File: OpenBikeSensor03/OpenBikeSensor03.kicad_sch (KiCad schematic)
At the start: 24 parts, among them J1 Battery, J2 GPS, J3 Sensor 1, J4 Sensor 2, J5 Display Cable, J6 Ein/Aus-Schalter, J7 SD_Card, J8 Addons, M1 LIPoChargerwithProtection, U1 ESP32 WROOM 30-Pin, U4 DCDC_fix

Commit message: More simplification
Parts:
- C2, C3: footprint Capacitors_THT:CP_Radial_D4.0mm_P1.50mm -> Custom_Modules:CP_Radial_D4.0mm_P1.50mm
- F1: footprint Fuse_Holders_and_Fuses:Fuse_TE5_Littlefuse-395Series -> Custom_Modules:Fuse
- J1: footprint Connector_PinHeader_2.54mm:PinHeader_1x02_P2.54mm_Vertical -> Custom_Modules:Connector_1x02
- J2: renamed from J6; footprint Connector_PinHeader_2.54mm:PinHeader_1x02_P2.54mm_Vertical -> Custom_Modules:Connector_1x02
- U1: footprint ESP32-DEVKITC-32D:MODULE_ESP32-DEVKITC-32C_SMDBACKUP -> ESP32-DEVKITC-32D:MODULE_ESP32-DEVKITC-32C_SMD_BOTH
- U2: renamed from U4; footprint Custom_Modules:MT3608_SEPIC_DCDC -> Custom_Modules:MT3608_SEPIC_DCDC_SMD
- renumbered D2 to D1, H3 to H1, H1 to H3, J7 to J5, J2 to J6, J5 to J7, R2 to R1, R3 to R2, R1 to R3, R6 to R4, R7 to R5
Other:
- note added: "Add-ons"
- note added: "Befestigungslöcher"
- note added: "Spannungsteiler zur Messung der Batteriespannung"
- note removed: "Addons"
- moved on the sheet: H1, H3, J1, J2

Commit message: clean up libraries
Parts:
- J2: value Ein/Aus-Schalter -> On/Off
- J3, J4: footprint Connector_PinHeader_2.54mm:PinHeader_1x04_P2.54mm_Vertical -> Custom_Modules:Connector_1x04
- J5: renamed from J7; footprint Connector_JST:JST_XH_B5B-XH-AM_1x05_P2.50mm_Vertical -> Custom_Modules:Connector_1x05_Display
- J6: renamed from J8; value Addons -> Add-ons; footprint Connector_PinHeader_2.54mm:PinHeader_1x06_P2.54mm_Vertical -> Custom_Modules:Connector_1x06
- M1: renamed from U1; footprint ESP32-DEVKITC-32D:MODULE_ESP32-DEVKITC-32C_SMD_BOTH -> Custom_Modules:ESP32_WROOM_30_SMD; symbol ESP32-DEVKITC-32D:ESP32-DEVKIT-32C -> Custom_Module:ESP32-WROOM-30
- M2: renamed from M1; symbol Custom_Module:LIPoChargerwithProtection -> Custom_Module:LIPoChargerWithProtection
- M3: renamed from U2; symbol DCDC_Converter:DCDC_fix -> Custom_Module:VoltageRegulator
- M4: renamed from J5; value SD_Card -> SD; footprint Connector_PinHeader_2.54mm:PinHeader_1x06_P2.54mm_Vertical -> Custom_Modules:Connector_1x06
- M5: renamed from J6; footprint Connector_PinHeader_2.54mm:PinHeader_1x04_P2.54mm_Vertical -> Custom_Modules:Connector_1x04
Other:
- note added: "Bulk decoupling, place near ESP32 and display cable connector"
- note added: "DC/DC voltage regulator (red module)"
- note added: "Distance Sensors"
- note added: "GPS Module"
- note added: "I2C pull up resistors"
- note added: "IN=USB Voltage, not used"
- note added: "LiPo Charger and Protection (blue module)"
- note added: "Mounting"
- note added: "Mounting holes"
- note added: "Passives"
- note added: "Power"
- note added: "SD Card Module"
- note added: "The addon port can be used for hacking the device and adding custom extensions, or while debugging. It exposes 3.3V power, the I2C bus and the RX/TX lines for serial output and communications."
- note added: "Voltage divider for measuring battery voltage via ADC pin"
- note added: "pull down resistor for button"
- note removed: "Befestigung"
- note removed: "Befestigungslöcher"
- note removed: "Entkopplung, platzieren in Nähe von ESP32 und Displaystecker"
- note removed: "GPS-Modul"
- note removed: "I2C Pull-Ups"
- note removed: "IN+/IN- ist die USB Bus-Spannung und wird nicht verwendet"
- note removed: "Laderegler & Batterieschutz (blaues Modul)"
- note removed: "Passive Bauteile"
- note removed: "Pull-Down Button"
- note removed: "SD-Karte"
- note removed: "Sensoren"
- note removed: "Spannungsregler (rotes Modul)"
- note removed: "Spannungsteiler zur Messung der Batteriespannung"
- note removed: "Stromversorgung"
- moved on the sheet: C1, C2, C3, D1, F1, H1, H2, H3, J1, J2, J3, J4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

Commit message: rename custom libraries to "OpenBikeSensor"
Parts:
- C2, C3: footprint Custom_Modules:CP_Radial_D4.0mm_P1.50mm -> OpenBikeSensor:CP_Radial_D4.0mm_P1.50mm
- F1: footprint Custom_Modules:Fuse -> OpenBikeSensor:Fuse
- J1, J2: footprint Custom_Modules:Connector_1x02 -> OpenBikeSensor:Connector_1x02
- J3, J4, M5: footprint Custom_Modules:Connector_1x04 -> OpenBikeSensor:Connector_1x04
- J5: footprint Custom_Modules:Connector_1x05_Display -> OpenBikeSensor:Connector_1x05_Display
- J6, M4: footprint Custom_Modules:Connector_1x06 -> OpenBikeSensor:Connector_1x06
- M1: footprint Custom_Modules:ESP32_WROOM_30_SMD -> OpenBikeSensor:ESP32_WROOM_30_SMD; symbol Custom_Module:ESP32-WROOM-30 -> OpenBikeSensor:ESP32-WROOM-30
- M2: footprint Custom_Modules:BATTERY-CHARGER-LI-PROT -> OpenBikeSensor:BATTERY-CHARGER-LI-PROT; symbol Custom_Module:LIPoChargerWithProtection -> OpenBikeSensor:LIPoChargerWithProtection
- M3: footprint Custom_Modules:MT3608_SEPIC_DCDC_SMD -> OpenBikeSensor:MT3608_SEPIC_DCDC_SMD; symbol Custom_Module:VoltageRegulator -> OpenBikeSensor:VoltageRegulator
- R1, R2, R3, R4, R5: footprint Custom_Modules:Resistor_Combined_THT3_SMD0805 -> OpenBikeSensor:Resistor_Combined_THT3_SMD0805

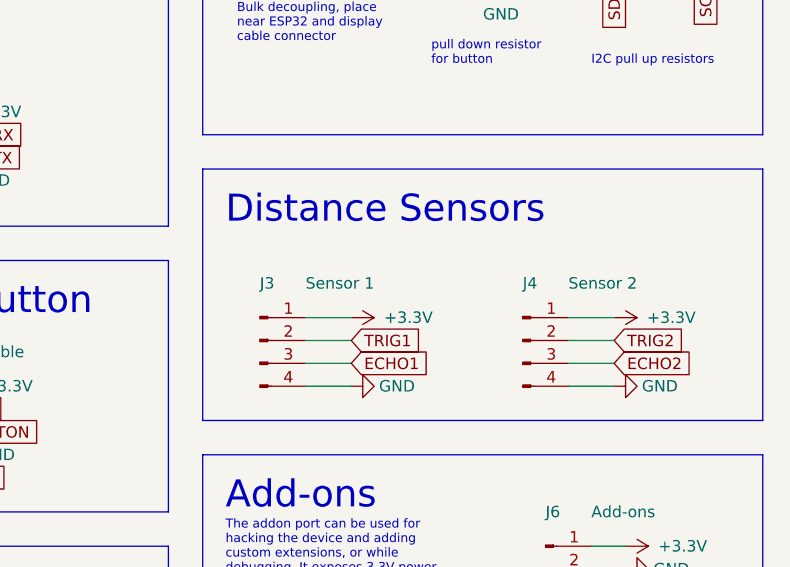
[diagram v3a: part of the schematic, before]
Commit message: Rename sensor module connectors to S1/S2
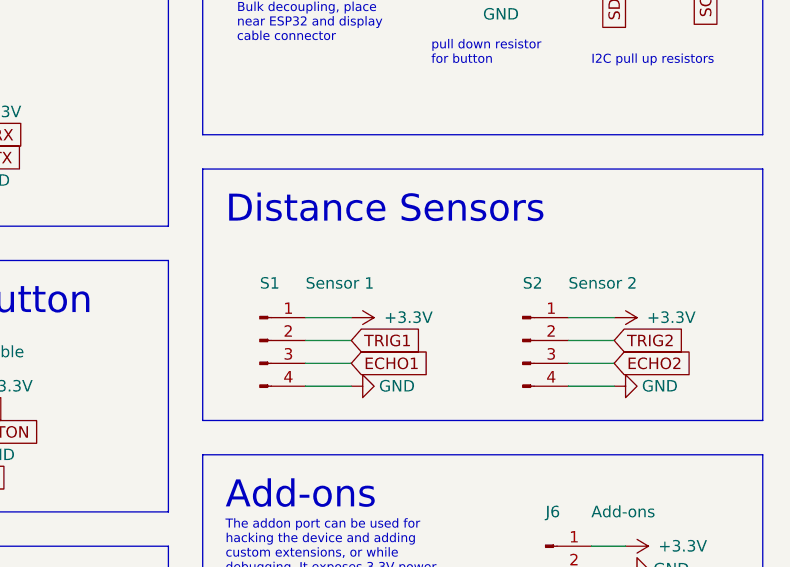
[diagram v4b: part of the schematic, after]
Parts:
- renumbered J3 to S1, J4 to S2
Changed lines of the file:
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@@
   (symbol (lib_id "Connector:Conn_01x04_Male") (at 212.09 101.6 0) (unit 1)
     (in_bom yes) (on_board yes)
-    (property "Reference" "J3" (id 0) (at 212.09 95.25 0)
+    (property "Reference" "S1" (id 0) (at 212.09 95.25 0)
       (effects (font (size 1.27 1.27)) (justify left))
     )
@@
   (symbol (lib_id "Connector:Conn_01x04_Male") (at 241.3 101.6 0) (unit 1)
     (in_bom yes) (on_board yes)
-    (property "Reference" "J4" (id 0) (at 241.3 95.25 0)
+    (property "Reference" "S2" (id 0) (at 241.3 95.25 0)
       (effects (font (size 1.27 1.27)) (justify left))
     )
@@
       (reference "J2") (unit 1) (value "On/Off") (footprint "OpenBikeSensor:Connector_1x02")
     )
-    (path "/00000000-0000-0000-0000-00005ed6a6b4"
-      (reference "J3") (unit 1) (value "Sensor 1") (footprint "OpenBikeSensor:Connector_1x04")
-    )
-    (path "/00000000-0000-0000-0000-00005ed6b21f"
-      (reference "J4") (unit 1) (value "Sensor 2") (footprint "OpenBikeSensor:Connector_1x04")
-    )
     (path "/00000000-0000-0000-0000-00005ed82c02"
       (reference "J5") (unit 1) (value "Display Cable") (footprint "OpenBikeSensor:Connector_1x05_Display")
@@
       (reference "R5") (unit 1) (value "1k2") (footprint "OpenBikeSensor:Resistor_Combined_THT3_SMD0805")
     )
-  )
+    (path "/00000000-0000-0000-0000-00005ed6a6b4"
+      (reference "S1") (unit 1) (value "Sensor 1") (footprint "OpenBikeSensor:Connector_1x04")
+    )
+    (path "/00000000-0000-0000-0000-00005ed6b21f"
+      (reference "S2") (unit 1) (value "Sensor 2") (footprint "OpenBikeSensor:Connector_1x04")
+    )
+  )
